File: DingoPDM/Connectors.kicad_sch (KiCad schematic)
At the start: 15 parts, among them J1 RedCubeTerminal, J2 USB_C_Receptacle_USB2.0, J3 1-776267-1, J4 1-776267-1, Q1 BC817-40

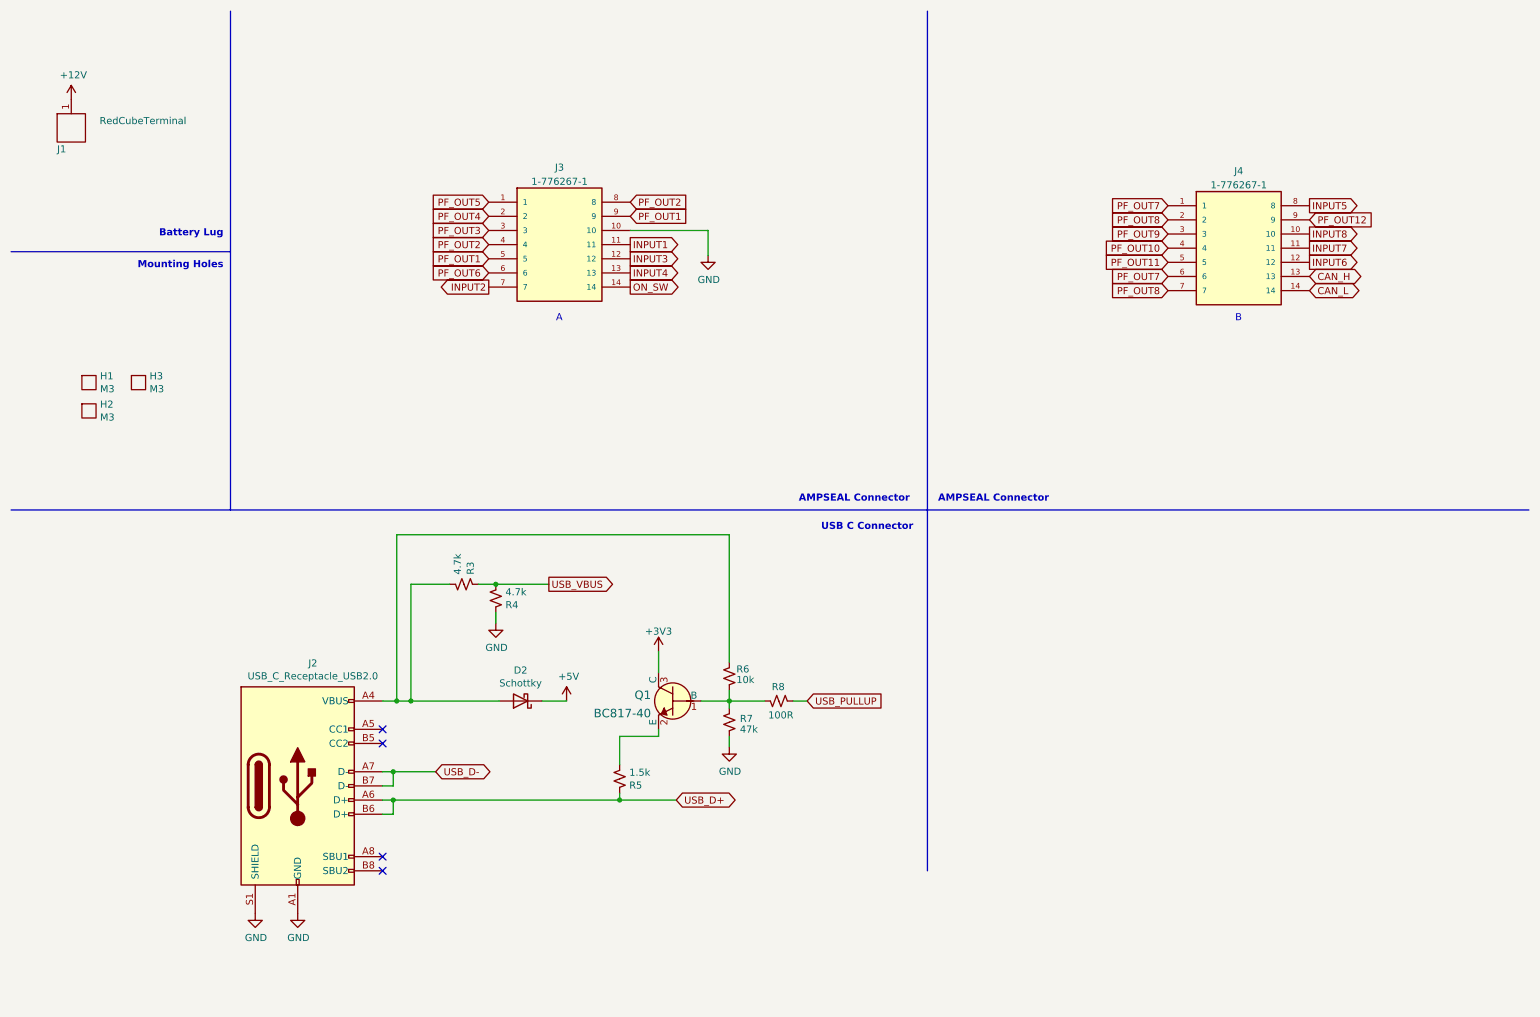
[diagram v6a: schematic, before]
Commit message: Changed schematic sheet size to letter
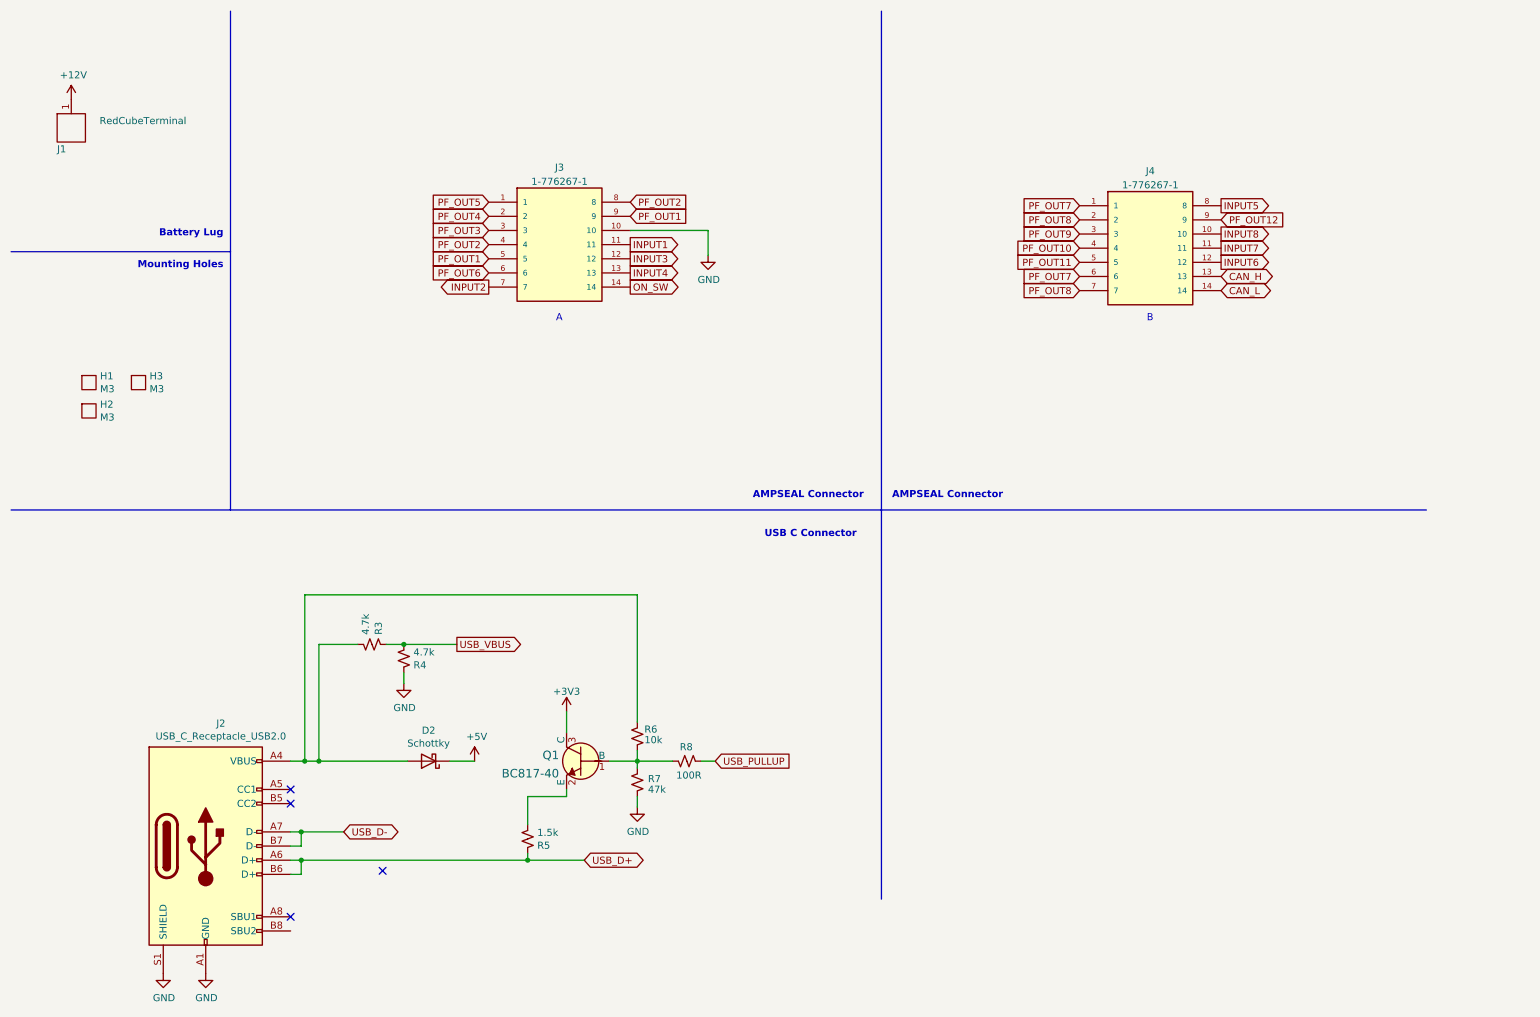
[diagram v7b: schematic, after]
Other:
- moved on the sheet: D2, J2, J4, Q1, R3, R4, R5, R6, R7, R8
